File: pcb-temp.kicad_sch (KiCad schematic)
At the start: 5 parts, among them J1 Conn_01x04_Pin, U1 BMP280

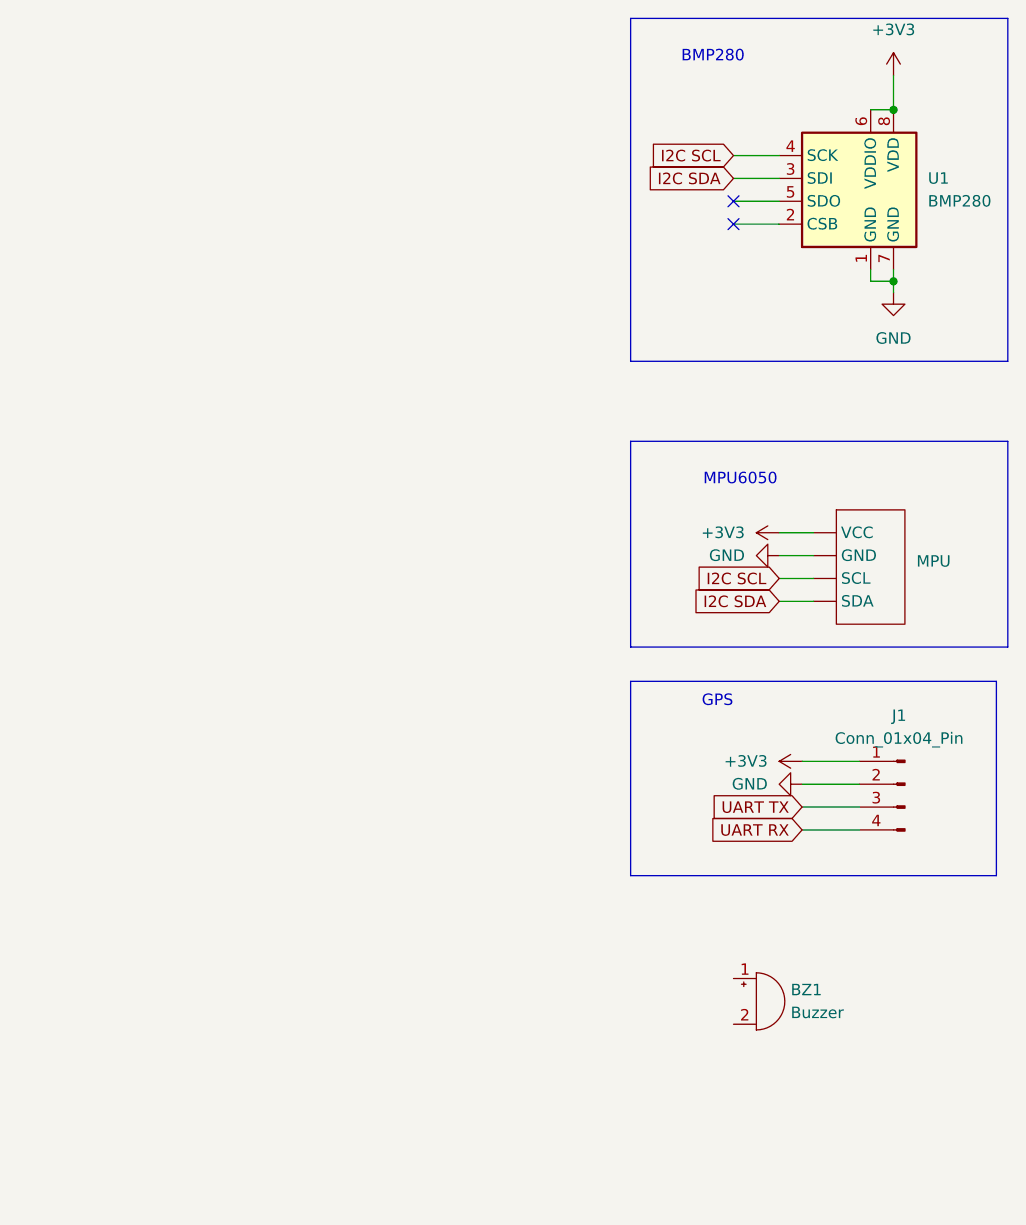
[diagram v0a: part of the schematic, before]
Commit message: added DSHOT, led, pyro channels
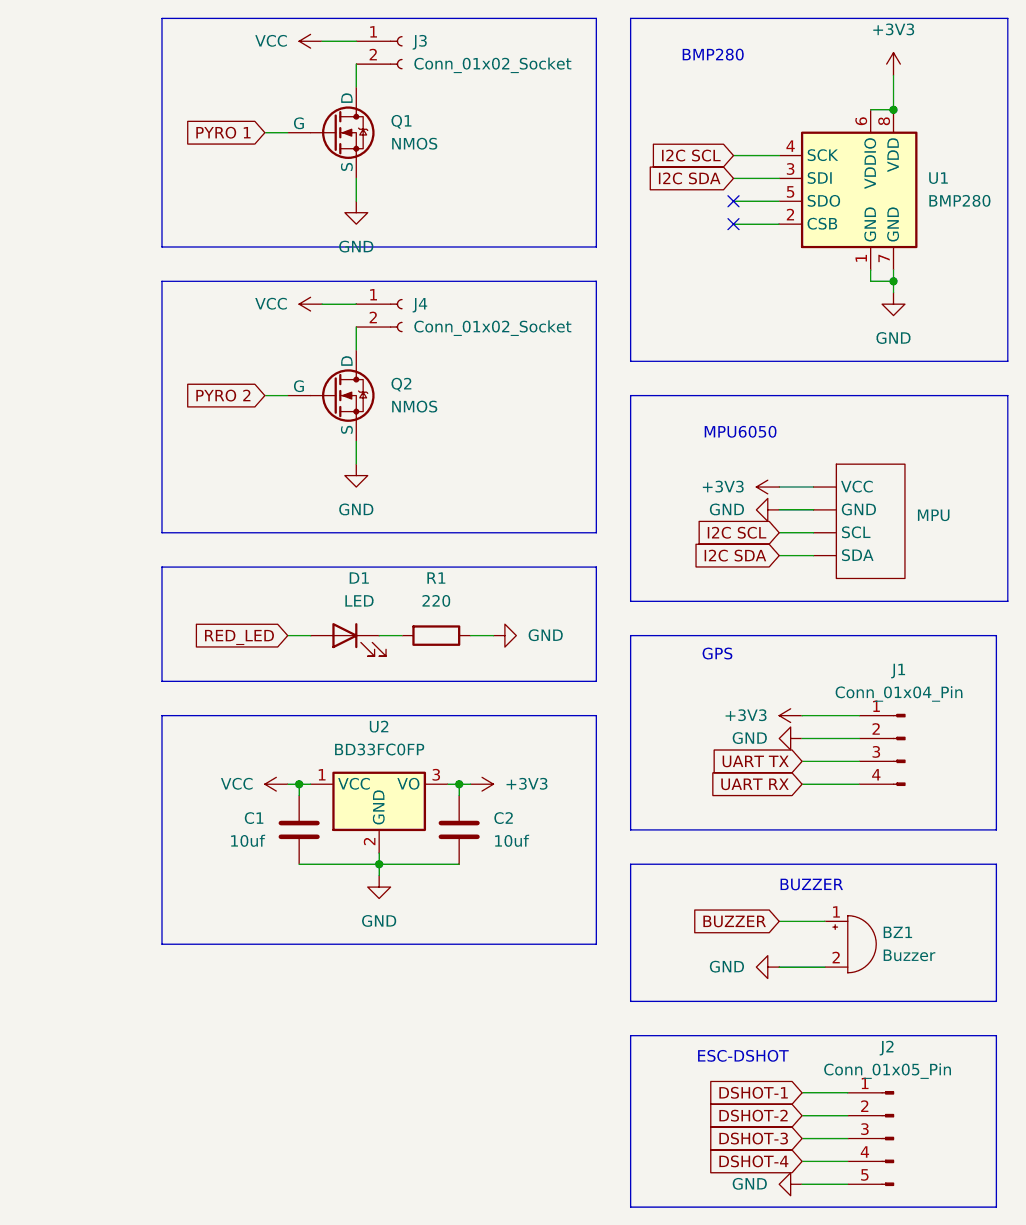
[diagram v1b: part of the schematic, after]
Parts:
- added C1, C2: 10uf, symbol Device:C
- added D1: LED, symbol Device:LED
- added J2: Conn_01x05_Pin, symbol Connector:Conn_01x05_Pin
- added J3, J4: Conn_01x02_Socket, symbol Connector:Conn_01x02_Socket
- added Q1, Q2: NMOS, symbol Simulation_SPICE:NMOS
- added R1: 220, symbol Device:R
- added U2: BD33FC0FP, Package_TO_SOT_SMD:TO-252-2, symbol Regulator_Linear:BD33FC0FP
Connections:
- net +3V3: now also C2.1, U2.3 (VO)
- net GND: now also BZ1.2 (-), C1.2, C2.2, J2.5 (Pin_5), Q1.3 (S), Q2.3 (S), R1.1, U2.2 (GND)
- net BUZZER: now reaches BZ1.1 (+)
- new net: J4.2 (Pin_2), Q2.1 (D)
- new net: D1.1 (K), R1.2
- new net: J3.2 (Pin_2), Q1.1 (D)
- new net DSHOT-1: J2.1 (Pin_1)
- new net DSHOT-2: J2.2 (Pin_2)
- new net DSHOT-3: J2.3 (Pin_3)
- new net DSHOT-4: J2.4 (Pin_4)
- new net PYRO 1: Q1.2 (G)
- new net PYRO 2: Q2.2 (G)
- new net RED_LED: D1.2 (A)
- new net VCC: C1.1, J3.1 (Pin_1), J4.1 (Pin_1), U2.1 (VCC)
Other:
- note added: "BUZZER"
- note added: "ESC-DSHOT"
- moved on the sheet: BZ1, J1, MPU

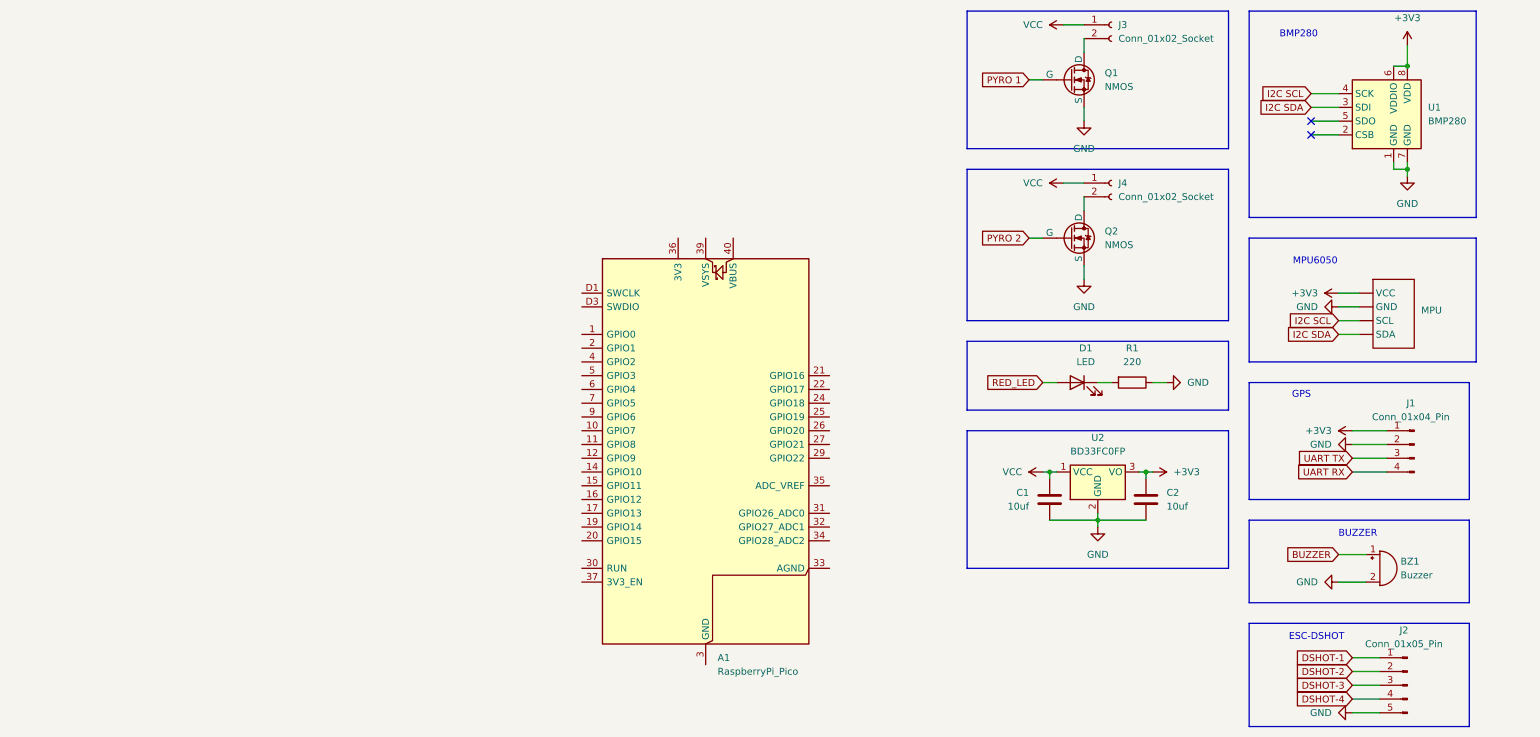
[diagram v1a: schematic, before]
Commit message: added LoRa and corrected connections
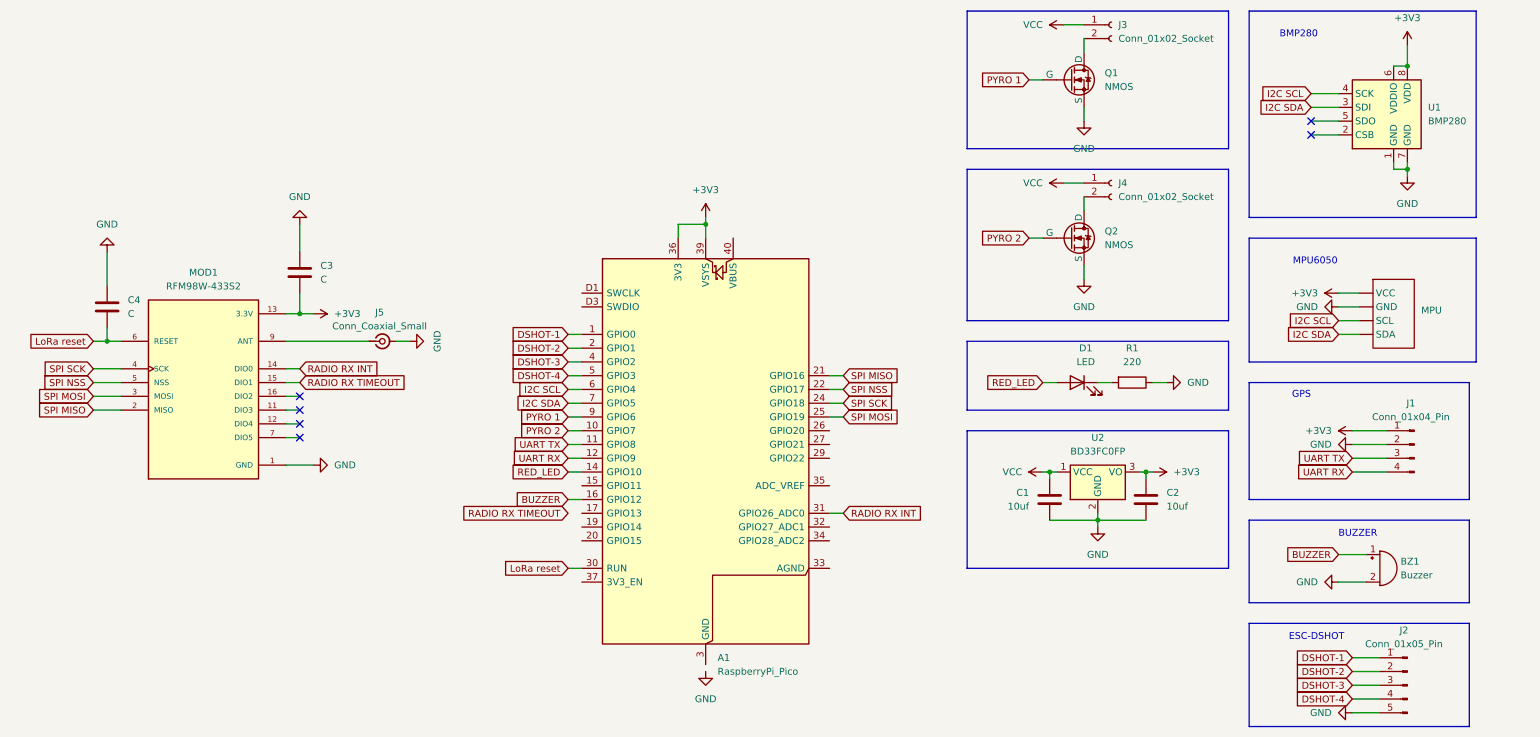
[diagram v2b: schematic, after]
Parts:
- added C3, C4: C, symbol Device:C
- added J5: Conn_Coaxial_Small, symbol Connector:Conn_Coaxial_Small
- added MOD1: RFM98W-433S2, RFM98W-433S2:XCVR_RFM98W-433S2, symbol RFM98W-433S2:RFM98W-433S2
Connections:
- net +3V3: now also A1.36 (3V3), A1.39 (VSYS), C3.2, MOD1.13 (3.3V), MOD1.13_1 (3.3V)
- net BUZZER: now also A1.16 (GPIO12)
- net DSHOT-1: now also A1.1 (GPIO0)
- net DSHOT-2: now also A1.2 (GPIO1)
- net DSHOT-3: now also A1.4 (GPIO2)
- net DSHOT-4: now also A1.5 (GPIO3)
- net GND: now also C3.1, C4.1, J5.2 (Ext), MOD1.1 (GND), MOD1.10 (GND), MOD1.10_1 (GND), MOD1.1_1 (GND), MOD1.8 (GND), MOD1.8_1 (GND)
- net I2C SCL: now also A1.6 (GPIO4)
- net I2C SDA: now also A1.7 (GPIO5)
- net PYRO 1: now also A1.9 (GPIO6)
- net PYRO 2: now also A1.10 (GPIO7)
- net RED_LED: now also A1.14 (GPIO10)
- net UART RX: now also A1.12 (GPIO9)
- net UART TX: now also A1.11 (GPIO8)
- net SPI MISO: now reaches A1.21 (GPIO16)
- net SPI MISO: now also MOD1.2 (MISO), MOD1.2_1 (MISO)
- net SPI NSS: now reaches A1.22 (GPIO17)
- net SPI NSS: now also MOD1.5 (NSS), MOD1.5_1 (NSS)
- net SPI SCK: now reaches A1.24 (GPIO18)
- net SPI SCK: now also MOD1.4 (SCK), MOD1.4_1 (SCK)
- net SPI MOSI: now reaches A1.25 (GPIO19)
- net SPI MOSI: now also MOD1.3 (MOSI), MOD1.3_1 (MOSI)
- net LoRa reset: now reaches A1.30 (RUN)
- net LoRa reset: now also C4.2, MOD1.6 (RESET), MOD1.6_1 (RESET)
- net RADIO RX INT: now reaches A1.31 (GPIO26_ADC0)
- net RADIO RX INT: now also MOD1.14 (DIO0), MOD1.14_1 (DIO0)
- new net: J5.1 (In), MOD1.9 (ANT), MOD1.9_1 (ANT)
- new net: MOD1.11 (DIO3), MOD1.11_1 (DIO3)
- new net: MOD1.12 (DIO4), MOD1.12_1 (DIO4)
- new net: MOD1.16 (DIO2), MOD1.16_1 (DIO2)
- new net: MOD1.7 (DIO5), MOD1.7_1 (DIO5)
- new net RADIO RX TIMEOUT: MOD1.15 (DIO1), MOD1.15_1 (DIO1)
- no-connect marks 2 -> 6

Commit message: changed pico's pinout and added ports to connect with other board
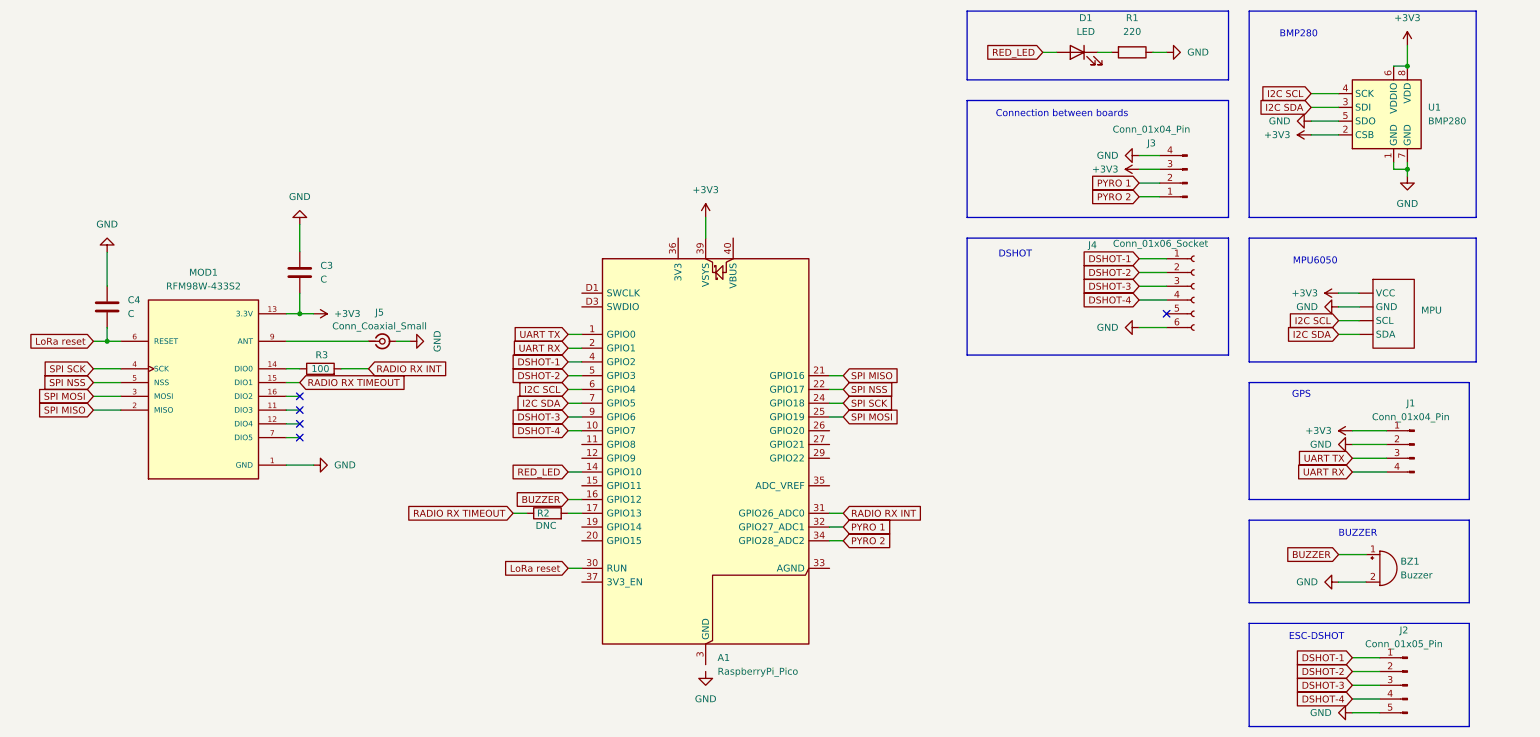
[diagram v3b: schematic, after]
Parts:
- removed C1, C2: 10uf, symbol Device:C
- removed J3, J4: Conn_01x02_Socket, symbol Connector:Conn_01x02_Socket
- removed Q1, Q2: NMOS, symbol Simulation_SPICE:NMOS
- removed U2: BD33FC0FP, Package_TO_SOT_SMD:TO-252-2, symbol Regulator_Linear:BD33FC0FP
- added J3: Conn_01x04_Pin, symbol Connector:Conn_01x04_Pin
- added J4: Conn_01x06_Socket, symbol Connector:Conn_01x06_Socket
- added R2: DNC, symbol Device:R
- added R3: 100, symbol Device:R
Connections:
- net +3V3: now also U1.2 (CSB), J3.3 (Pin_3); no longer A1.36 (3V3)
- net DSHOT-1: now also A1.4 (GPIO2), J4.1 (Pin_1); no longer A1.1 (GPIO0)
- net DSHOT-2: now also A1.5 (GPIO3), J4.2 (Pin_2); no longer A1.2 (GPIO1)
- net DSHOT-3: now also A1.9 (GPIO6), J4.3 (Pin_3); no longer A1.4 (GPIO2)
- net DSHOT-4: now also A1.10 (GPIO7), J4.4 (Pin_4); no longer A1.5 (GPIO3)
- net GND: now also U1.5 (SDO), J3.4 (Pin_4), J4.6 (Pin_6)
- net PYRO 1: now also A1.32 (GPIO27_ADC1), J3.2 (Pin_2); no longer A1.9 (GPIO6)
- net PYRO 2: now also A1.34 (GPIO28_ADC2), J3.1 (Pin_1); no longer A1.10 (GPIO7)
- net RADIO RX INT: now also R3.2; no longer MOD1.14 (DIO0), MOD1.14_1 (DIO0)
- net RADIO RX TIMEOUT: now also R2.1
- net UART RX: now also A1.2 (GPIO1); no longer A1.12 (GPIO9)
- net UART TX: now also A1.1 (GPIO0); no longer A1.11 (GPIO8)
- net at A1.17 (GPIO13): now also R2.2
- new net: MOD1.14 (DIO0), MOD1.14_1 (DIO0), R3.1
- no-connect marks 6 -> 5
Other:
- note added: "Connection between boards"
- note added: "DSHOT"
- moved on the sheet: D1, R1

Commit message: finished pcb layout'
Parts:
- removed J2: Conn_01x05_Pin, symbol Connector:Conn_01x05_Pin
- removed MPU: ~, symbol MPU6050_USED:MPU6050-USED
- removed R2: DNC, symbol Device:R
- removed U1: BMP280, Charleslabs_Parts:BMP280_Module, symbol Sensor_Pressure:BMP280
- added A2: BMP280_Module, Charleslabs_Parts:BMP280_Module, symbol Charleslabs_Parts:BMP280_Module
- added C1: 100u, Capacitor_THT:CP_Radial_D5.0mm_P2.50mm, symbol Device:C
- added MPU1: ~, Sensor_Motion:MPU6050, symbol MPU6050_USED:MPU6050-USED
- BZ1: footprint (none) -> Buzzer_Beeper:Buzzer_15x7.5RM7.6
- C3: value C -> 100u; footprint (none) -> Capacitor_THT:CP_Radial_D5.0mm_P2.50mm
- C4: value C -> 100n; footprint (none) -> Capacitor_THT:CP_Radial_D4.0mm_P1.50mm
- D1: footprint (none) -> LED_THT:LED_D4.0mm
- J1: footprint (none) -> Connector_PinSocket_2.54mm:PinSocket_1x04_P2.54mm_Vertical
- J2: renamed from J3; footprint (none) -> Connector_PinSocket_2.54mm:PinSocket_1x04_P2.54mm_Vertical
- J3: renamed from J4; footprint (none) -> Connector_JST:JST_EH_B6B-EH-A_1x06_P2.50mm_Vertical
- J5: footprint (none) -> Connector_Coaxial:SMA_Amphenol_901-144_Vertical
- R1, R3: footprint (none) -> Resistor_THT:R_Axial_DIN0309_L9.0mm_D3.2mm_P12.70mm_Horizontal
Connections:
- net +3V3: now also A2.1 (VCC), C1.2, MPU1.1 (VCC)
- net GND: now also A1.13 (GND), A1.18 (GND), A1.23 (GND), A1.28 (GND), A1.3 (GND), A1.38 (GND), A1.8 (GND), A1.D2 (GND), A2.2 (GND), C1.1, MPU1.2 (GND)
- net I2C SCL: now also A2.3 (SCL), MPU1.3 (SCL)
- net I2C SDA: now also A2.4 (SDA), MPU1.4 (SDA)
- no-connect marks 5 -> 28
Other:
- note removed: "ESC-DSHOT"
- moved on the sheet: BZ1, J1

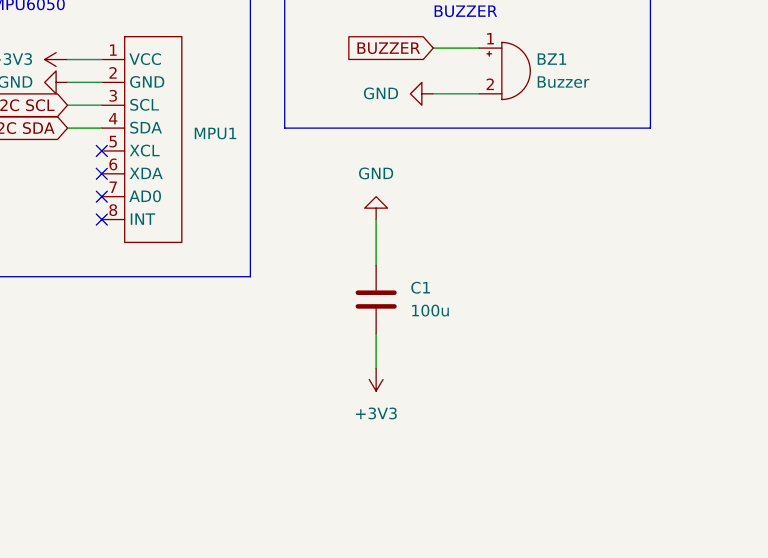
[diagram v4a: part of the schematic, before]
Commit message: thickened 3V3 path
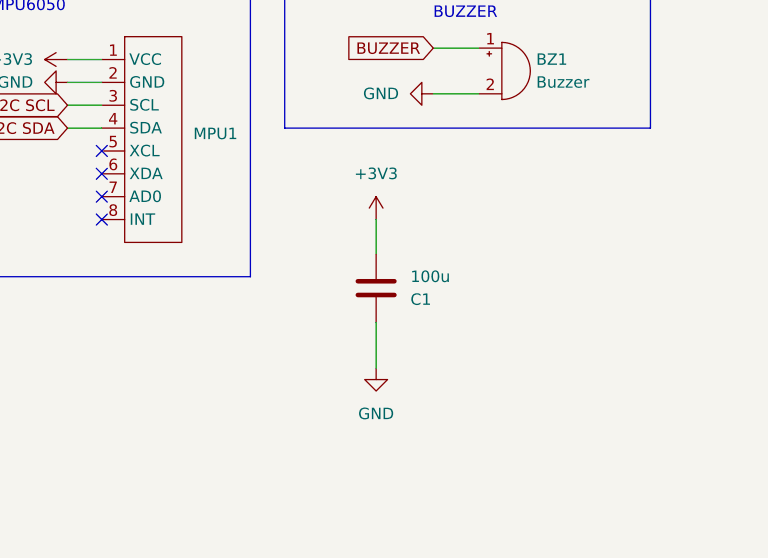
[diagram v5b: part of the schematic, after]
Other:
- moved on the sheet: C1
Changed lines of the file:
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@@
 	(wire
 		(pts
-			(xy 251.46 119.38) (xy 251.46 123.19)
+			(xy 251.46 110.49) (xy 251.46 106.68)
 		)
 		(stroke
@@
 	(wire
 		(pts
-			(xy 251.46 106.68) (xy 251.46 111.76)
+			(xy 251.46 123.19) (xy 251.46 118.11)
 		)
 		(stroke
@@
 	(symbol
 		(lib_id "power:+3V3")
-		(at 251.46 123.19 180)
+		(at 251.46 106.68 0)
+		(mirror y)
 		(unit 1)
 		(exclude_from_sim no)
@@
 		(fields_autoplaced yes)
 		(property "Reference" "#PWR014"
-			(at 251.46 119.38 0)
+			(at 251.46 110.49 0)
 			(effects
 				(font
@@
 		)
 		(property "Value" "+3V3"
-			(at 251.46 128.27 0)
+			(at 251.46 101.6 0)
 			(effects
 				(font
@@
 		)
 		(property "Footprint" ""
-			(at 251.46 123.19 0)
+			(at 251.46 106.68 0)
 			(effects
 				(font
@@
 		)
 		(property "Datasheet" ""
-			(at 251.46 123.19 0)
+			(at 251.46 106.68 0)
 			(effects
 				(font
@@
 		)
 		(property "Description" "Power symbol creates a global label with name \"+3V3\""
-			(at 251.46 123.19 0)
+			(at 251.46 106.68 0)
 			(effects
 				(font
@@
 	(symbol
 		(lib_id "Device:C")
-		(at 251.46 115.57 0)
+		(at 251.46 114.3 0)
+		(mirror x)
 		(unit 1)
 		(exclude_from_sim no)
@@
 		(fields_autoplaced yes)
 		(property "Reference" "C1"
-			(at 255.27 114.2999 0)
+			(at 255.27 115.5701 0)
 			(effects
 				(font
@@
 		)
 		(property "Value" "100u"
-			(at 255.27 116.8399 0)
+			(at 255.27 113.0301 0)
 			(effects
 				(font
@@
 		)
 		(property "Footprint" "Capacitor_THT:CP_Radial_D5.0mm_P2.50mm"
-			(at 252.4252 119.38 0)
+			(at 252.4252 110.49 0)
 			(effects
 				(font
@@
 		)
 		(property "Datasheet" "~"
-			(at 251.46 115.57 0)
+			(at 251.46 114.3 0)
 			(effects
 				(font
@@
 		)
 		(property "Description" "Unpolarized capacitor"
-			(at 251.46 115.57 0)
+			(at 251.46 114.3 0)
 			(effects
 				(font
@@
 	(symbol
 		(lib_id "power:GND")
-		(at 251.46 106.68 0)
-		(mirror x)
+		(at 251.46 123.19 0)
 		(unit 1)
 		(exclude_from_sim no)
@@
 		(dnp no)
 		(property "Reference" "#PWR08"
-			(at 251.46 100.33 0)
+			(at 251.46 129.54 0)
 			(effects
 				(font
@@
 		)
 		(property "Value" "GND"
-			(at 251.46 101.6 0)
+			(at 251.46 128.27 0)
 			(effects
 				(font
@@
 		)
 		(property "Footprint" ""
-			(at 251.46 106.68 0)
+			(at 251.46 123.19 0)
 			(effects
 				(font
@@
 		)
 		(property "Datasheet" ""
-			(at 251.46 106.68 0)
+			(at 251.46 123.19 0)
 			(effects
 				(font
@@
 		)
 		(property "Description" "Power symbol creates a global label with name \"GND\" , ground"
-			(at 251.46 106.68 0)
+			(at 251.46 123.19 0)
 			(effects
 				(font
